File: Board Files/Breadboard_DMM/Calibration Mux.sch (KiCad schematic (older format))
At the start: 3 parts

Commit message: Finished main design, cleaning up schematic
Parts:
- added D?: 1N4007, Diode_SMD:D_SOD-123, symbol Device:D_ALT
- added K? (x2): EC2-5NU, Relay_THT:Relay_DPDT_Kemet_EC2, symbol irex_Relay:EC2-5NU_Split
- added Q? (x3): NTZD3154N, Package_TO_SOT_SMD:SOT-563, symbol irex_Transistor_FET:NTZD3154N
- added R? (x3): 10k, symbol Device:R_US
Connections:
- net +5VA: now also D?.1 (K), K?.1, R?.1, R?.1
- net GND: now also Q?.1 (S1), Q?.1 (S1), Q?.4 (S2), R?.2
- net INPUT_V+: now also K?.3; no longer U?.13 (X-COM)
- net CALIBRATE_MUX_A: no longer names the net of U?.10 (A)
- net CALIBRATE_MUX_A: now also Q?.6 (D1), R?.2
- net CALIBRATE_MUX_B: no longer names the net of U?.9 (B)
- net CALIBRATE_MUX_B: now also Q?.3 (D2), R?.2
- net CALIBRATE_MUX_INH: no longer names the net of R?.1, U?.6 (INH)
- new net: K?.5, U?.13 (X-COM)
- new net: D?.2 (A), K?.12, Q?.6 (D1)
- new net CALIBRATE_MUX_~A: Q?.2 (G1)
- new net CALIBRATE_MUX_~B: Q?.5 (G2)
- new net CALIBRATE_RELAY_ON: Q?.2 (G1), R?.1
- new net OUTPUT_V+: K?.4
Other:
- note added: "Calibration Input\nSelector"
- note added: "Calibration Relay Coil"
- note added: "~A"
- note added: "~B\n"
- note removed: "A"
- note removed: "B\n"
- moved on the sheet: C?, R?, U?

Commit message: Finished main cleanup, started adding digikey part numbers
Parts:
- C601: renamed from C?; Digi-Key PN (none) -> -
- D601: renamed from D?; Digi-Key PN (none) -> -
- K601: renamed from K?; Digi-Key PN (none) -> -
- Q601, Q602: renamed from Q?; Digi-Key PN (none) -> -
- R601, R602, R603, R604: renamed from R?; Digi-Key PN (none) -> -
- U601: renamed from U?; Digi-Key PN (none) -> -

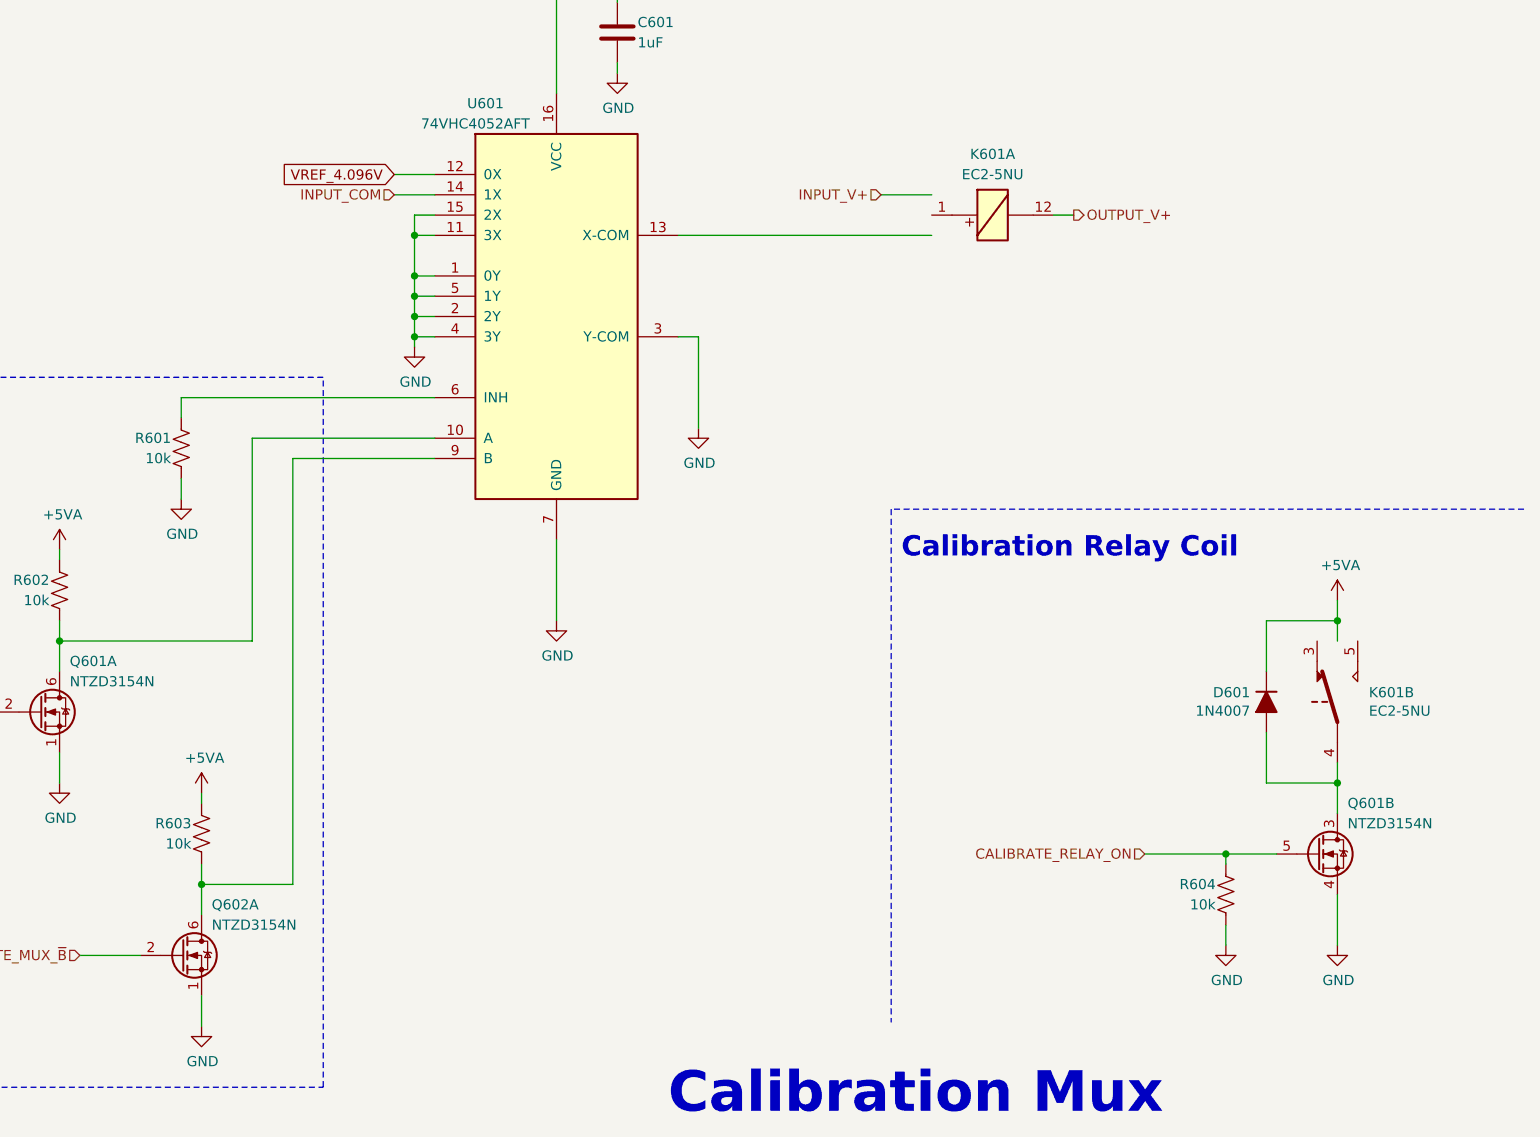
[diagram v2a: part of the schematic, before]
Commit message: Started adding Digikey links
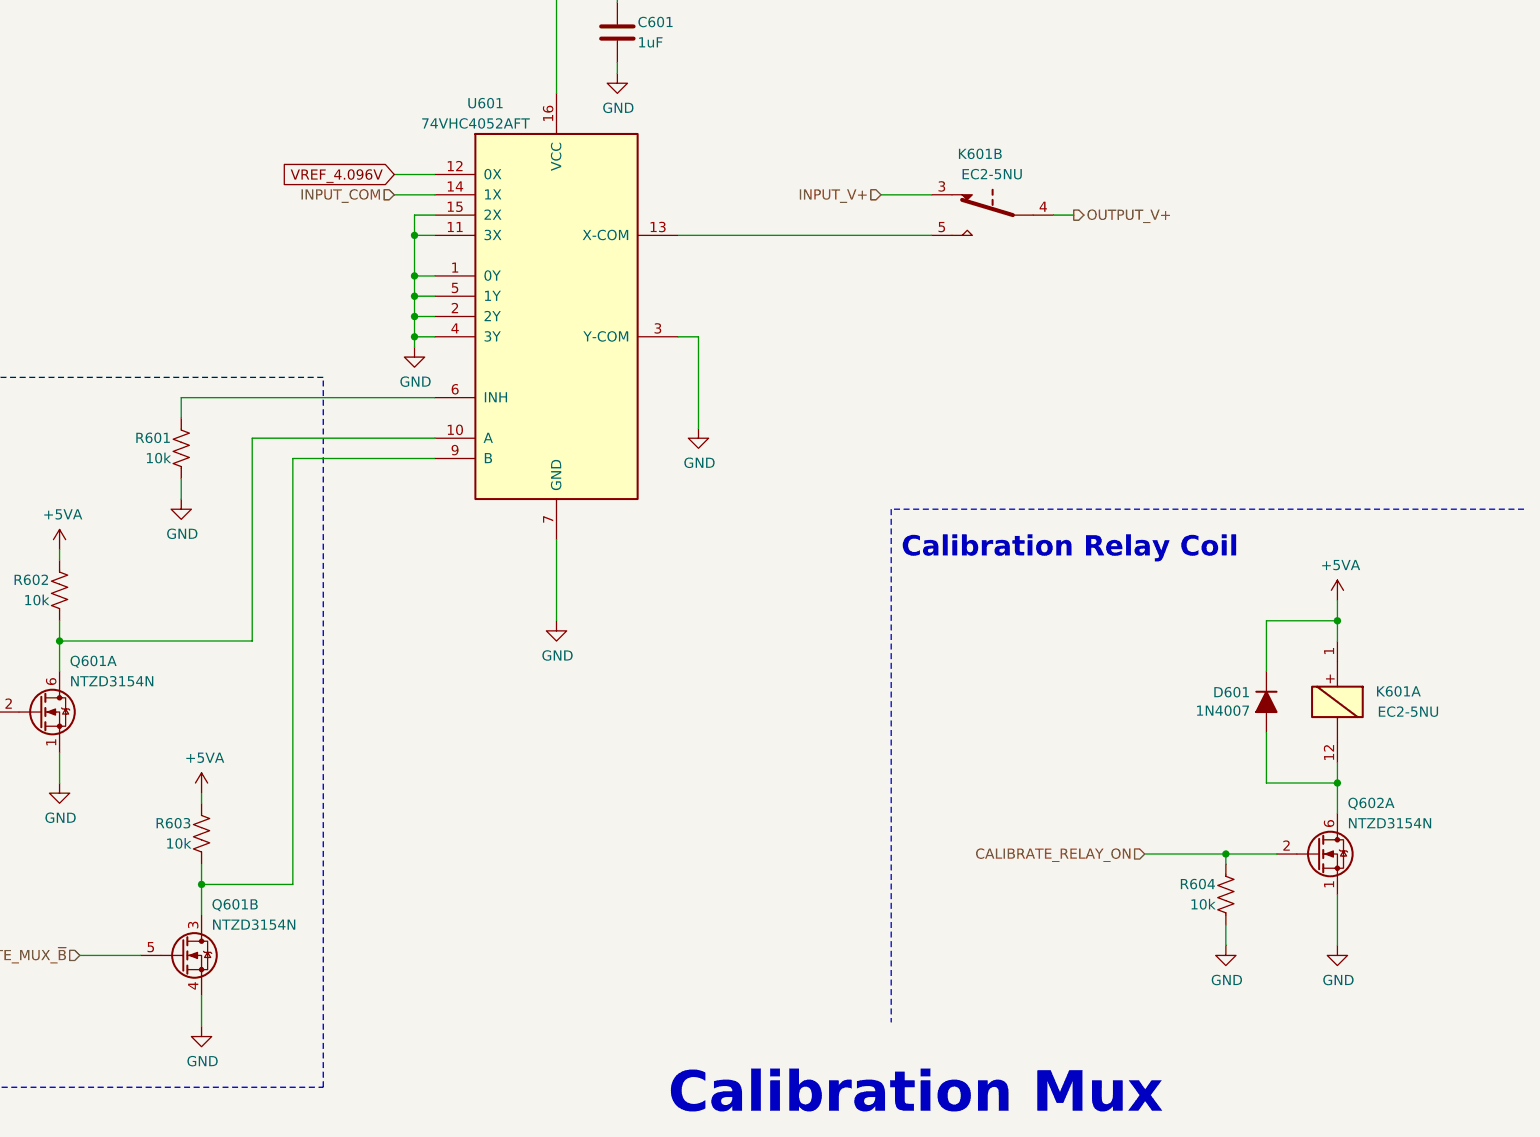
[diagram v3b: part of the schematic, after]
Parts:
- D601: Digi-Key Link (none) -> https://www.digikey.com/en/products/detail/smc-diode-soluti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; Digi-Key PN - -> 1655-1N4007FLCT-ND
- Q601: Digi-Key Link (none) -> https://www.digikey.com/en/products/detail/on-semiconductor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; Digi-Key PN - -> NTZD3154NT1GOSCT-ND
- Q601: renamed from Q602; Digi-Key Link (none) -> https://www.digikey.com/en/products/detail/on-semiconductor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; Digi-Key PN - -> NTZD3154NT1GOSCT-ND
- Q602: renamed from Q601; Digi-Key Link (none) -> https://www.digikey.com/en/products/detail/on-semiconductor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; Digi-Key PN - -> NTZD3154NT1GOSCT-ND
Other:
- moved on the sheet: K601A, K601B
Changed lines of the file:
@@
 $Descr USLetter 11000 8500
 encoding utf-8
-Sheet 5 10
+Sheet 6 11
 Title "Toast-O-Meter"
-Date ""
+Date "2020-08-14"
 Rev "0"
 Comp ""
@@
 $Comp
 L irex_Transistor_FET:NTZD3154N Q?
-U 1 1 5FFA77CB
+U 2 1 5FFA77CB
 P 4000 6450
 AR Path="/5F3FD151/5FFA77CB" Ref="Q?"  Part="2"
@@
 AR Path="/5F3FD151/5FEE79D7/5FFA77CB" Ref="Q?"  Part="2"
 AR Path="/5F511849/5F4FBB9F/5FEE8CDB/5FFA77CB" Ref="Q?"  Part="2"
-AR Path="/5F511849/5F4FBB9F/5FFA77CB" Ref="Q602"  Part="1"
-F 0 "Q602" H 4050 6700 50  0000 L CNN
+AR Path="/5F511849/5F4FBB9F/5FFA77CB" Ref="Q601"  Part="2"
+F 0 "Q601" H 4050 6700 50  0000 L CNN
 F 1 "NTZD3154N" H 4050 6600 50  0000 L CNN
 F 2 "Package_TO_SOT_SMD:SOT-563" H 4100 6350 50  0001 L CNN
 F 3 "https://www.onsemi.cn/PowerSolutions/document/NTZD3154N-D.PDF" H 4000 6450 50  0001 L CNN
-F 4 "" H 4000 6450 50  0001 C CNN "Digi-Key Link"
-F 5 "-" H 4000 6450 50  0001 C CNN "Digi-Key PN"
-	1    4000 6450
+F 4 "https://www.digikey.com/en/products/detail/on-semiconductor/NTZD3154NT1G/687137" H 4000 6450 50  0001 C CNN "Digi-Key Link"
+F 5 "NTZD3154NT1GOSCT-ND" H 4000 6450 50  0001 C CNN "Digi-Key PN"
+	2    4000 6450
 	1    0    0    -1
 $EndComp
@@
 F 2 "Package_TO_SOT_SMD:SOT-563" H 3400 5150 50  0001 L CNN
 F 3 "https://www.onsemi.cn/PowerSolutions/document/NTZD3154N-D.PDF" H 3300 5250 50  0001 L CNN
-F 4 "" H 3300 5250 50  0001 C CNN "Digi-Key Link"
-F 5 "-" H 3300 5250 50  0001 C CNN "Digi-Key PN"
+F 4 "https://www.digikey.com/en/products/detail/on-semiconductor/NTZD3154NT1G/687137" H 3300 5250 50  0001 C CNN "Digi-Key Link"
+F 5 "NTZD3154NT1GOSCT-ND" H 3300 5250 50  0001 C CNN "Digi-Key PN"
 	1    3300 5250
 	1    0    0    -1
@@
 $Comp
 L irex_Transistor_FET:NTZD3154N Q?
-U 2 1 5FFCC6C6
+U 1 1 5FFCC6C6
 P 9600 5950
 AR Path="/5F3FD151/5FFCC6C6" Ref="Q?"  Part="1"
@@
 AR Path="/5F511849/5F4FBB9F/5FEF5786/5FFCC6C6" Ref="Q?"  Part="1"
 AR Path="/5F511849/5F4FBB9F/5FEF9BAE/5FFCC6C6" Ref="Q?"  Part="1"
-AR Path="/5F511849/5F4FBB9F/5FFCC6C6" Ref="Q601"  Part="2"
-F 0 "Q601" H 9650 6200 50  0000 L CNN
+AR Path="/5F511849/5F4FBB9F/5FFCC6C6" Ref="Q602"  Part="1"
+F 0 "Q602" H 9650 6200 50  0000 L CNN
 F 1 "NTZD3154N" H 9650 6100 50  0000 L CNN
 F 2 "Package_TO_SOT_SMD:SOT-563" H 9700 5850 50  0001 L CNN
 F 3 "https://www.onsemi.cn/PowerSolutions/document/NTZD3154N-D.PDF" H 9600 5950 50  0001 L CNN
-F 4 "" H 9600 5950 50  0001 C CNN "Digi-Key Link"
-F 5 "-" H 9600 5950 50  0001 C CNN "Digi-Key PN"
-	2    9600 5950
+F 4 "https://www.digikey.com/en/products/detail/on-semiconductor/NTZD3154NT1G/687137" H 9600 5950 50  0001 C CNN "Digi-Key Link"
+F 5 "NTZD3154NT1GOSCT-ND" H 9600 5950 50  0001 C CNN "Digi-Key PN"
+	1    9600 5950
 	1    0    0    -1
 $EndComp
@@
 L irex_Relay:EC2-5NU_Split K?
 U 1 1 5FAFCC09
-P 7900 2800
+P 9600 5200
 AR Path="/5FAFCC09" Ref="K?"  Part="2"
 AR Path="/5F511849/5FAFCC09" Ref="K?"  Part="2"
 AR Path="/5F511849/5F4FBB9F/5FAFCC09" Ref="K601"  Part="1"
-F 0 "K601" V 7600 2800 50  0000 C CNN
-F 1 "EC2-5NU" V 7700 2800 50  0000 C CNN
+F 0 "K601" H 9300 5250 50  0000 C CNN
+F 1 "EC2-5NU" H 9250 5150 50  0000 C CNN
+F 2 "Relay_THT:Relay_DPDT_Kemet_EC2" H 9800 5100 50  0001 L CNN
+F 3 "https://content.kemet.com/datasheets/KEM_R7002_EC2_EE2.pdf" H 9600 5200 50  0001 C CNN
+F 4 "" H 9600 5200 50  0001 C CNN "Digi-Key Link"
+F 5 "-" H 9600 5200 50  0001 C CNN "Digi-Key PN"
+	1    9600 5200
+	-1   0    0    -1
+$EndComp
+$Comp
+L irex_Relay:EC2-5NU_Split K?
+U 2 1 5FAFCC0F
+P 7900 2800
+AR Path="/5FAFCC0F" Ref="K?"  Part="1"
+AR Path="/5F511849/5FAFCC0F" Ref="K?"  Part="1"
+AR Path="/5F511849/5F4FBB9F/5FAFCC0F" Ref="K601"  Part="2"
+F 0 "K601" V 7600 2750 50  0000 L CNN
+F 1 "EC2-5NU" V 7700 2650 50  0000 L CNN
 F 2 "Relay_THT:Relay_DPDT_Kemet_EC2" H 8100 2700 50  0001 L CNN
 F 3 "https://content.kemet.com/datasheets/KEM_R7002_EC2_EE2.pdf" H 7900 2800 50  0001 C CNN
 F 4 "" H 7900 2800 50  0001 C CNN "Digi-Key Link"
 F 5 "-" H 7900 2800 50  0001 C CNN "Digi-Key PN"
-	1    7900 2800
+	2    7900 2800
 	0    -1   1    0
-$EndComp
-$Comp
-L irex_Relay:EC2-5NU_Split K?
-U 2 1 5FAFCC0F
-P 9600 5200
-AR Path="/5FAFCC0F" Ref="K?"  Part="1"
-AR Path="/5F511849/5FAFCC0F" Ref="K?"  Part="1"
-AR Path="/5F511849/5F4FBB9F/5FAFCC0F" Ref="K601"  Part="2"
-F 0 "K601" H 9755 5246 50  0000 L CNN
-F 1 "EC2-5NU" H 9755 5155 50  0000 L CNN
-F 2 "Relay_THT:Relay_DPDT_Kemet_EC2" H 9800 5100 50  0001 L CNN
-F 3 "https://content.kemet.com/datasheets/KEM_R7002_EC2_EE2.pdf" H 9600 5200 50  0001 C CNN
-F 4 "" H 9600 5200 50  0001 C CNN "Digi-Key Link"
-F 5 "-" H 9600 5200 50  0001 C CNN "Digi-Key PN"
-	2    9600 5200
-	1    0    0    -1
 $EndComp
 $Comp
@@
 F 2 "Diode_SMD:D_SOD-123" H 9250 5200 50  0001 C CNN
 F 3 "http://www.smc-diodes.com/propdf/1N4001FL-1N4007FL%20N1646%20REV.A.pdf" H 9250 5200 50  0001 C CNN
-F 4 "" H 9250 5200 50  0001 C CNN "Digi-Key Link"
-F 5 "-" H 9250 5200 50  0001 C CNN "Digi-Key PN"
+F 4 "https://www.digikey.com/en/products/detail/smc-diode-solutions/1N4007FLTR/11657817" H 9250 5200 50  0001 C CNN "Digi-Key Link"
+F 5 "1655-1N4007FLCT-ND" H 9250 5200 50  0001 C CNN "Digi-Key PN"
 	1    9250 5200
 	0    -1   1    0

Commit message: Finished adding parts, cleaned up, ran ERC
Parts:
- added unit 2 of Q602
- added R603, R605, R606: 100, Resistor_SMD:R_0603_1608Metric_Pad1.05x0.95mm_HandSolder, symbol Device:R_US
- C601: footprint (none) -> Resistor_SMD:R_0603_1608Metric_Pad1.05x0.95mm_HandSolder; Digi-Key Link (none) -> https://www.digikey.com/en/products/detail/samsung-electro-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; Digi-Key PN - -> 1276-6524-1-ND
- K601: Digi-Key Link (none) -> https://www.digikey.com/en/products/detail/kemet/EC2-5NU/42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; Digi-Key PN - -> 399-11052-5-ND
- R601, R602: footprint (none) -> Resistor_SMD:R_0603_1608Metric_Pad1.05x0.95mm_HandSolder; Digi-Key Link (none) -> https://www.digikey.com/en/products/detail/yageo/RC0603FR-0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; Digi-Key PN - -> 311-10.0KHRCT-ND
- R604: renamed from R603; footprint (none) -> Resistor_SMD:R_0603_1608Metric_Pad1.05x0.95mm_HandSolder; Digi-Key Link (none) -> https://www.digikey.com/en/products/detail/yageo/RC0603FR-0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; Digi-Key PN - -> 311-10.0KHRCT-ND
- R607: renamed from R604; footprint (none) -> Resistor_SMD:R_0603_1608Metric_Pad1.05x0.95mm_HandSolder; Digi-Key Link (none) -> https://www.digikey.com/en/products/detail/yageo/RC0603FR-0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; Digi-Key PN - -> 311-10.0KHRCT-ND
- U601: Digi-Key Link (none) -> https://www.digikey.com/en/products/detail/toshiba-semicond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; Digi-Key PN - -> 74VHC4052AFTCT-ND
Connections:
- net CALIBRATE_MUX_~A: now also R603.1; no longer Q601.2 (G1)
- net CALIBRATE_MUX_~B: now also R606.1; no longer Q601.5 (G2)
- net CALIBRATE_RELAY_ON: now also R605.1; no longer Q602.2 (G1), R607.1
- net GND: now also Q602.3 (D2), Q602.4 (S2), Q602.5 (G2)
- new net: Q601.5 (G2), R606.2
- new net: Q601.2 (G1), R603.2
- new net: Q602.2 (G1), R605.2, R607.1
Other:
- moved on the sheet: C601, D601, K601A, K601B, Q601A, Q601B, Q602A, R601, R602, R604, R607, U601

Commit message: Updated probe connector arrangement
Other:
- note removed: "Calibration Mux"
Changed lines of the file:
@@
 Sheet 5 8
 Title "Toast-O-Meter"
-Date "2020-08-14"
+Date "2020-10-06"
 Rev "0"
 Comp ""
-Comment1 ""
+Comment1 "Isaac Rex"
 Comment2 ""
 Comment3 ""
 Comment4 ""
 $EndDescr
-Text Notes 12450 9700 0    200  ~ 40
-Calibration Mux
 Text Notes 4350 6250 0    50   ~ 0
 GND
@@
 Wire Wire Line
 	15050 8400 15300 8400
-Wire Notes Line
-	16520 6700 13400 6700
-Wire Notes Line
-	13400 6700 13400 9230
 $Comp
 L Device:R_US R?
@@
 	13950 7150 13950 7250
 Connection ~ 13550 7450
+Wire Notes Line
+	16500 6650 13200 6650
+Wire Notes Line
+	13200 6650 13200 9550
 $EndSCHEMATC

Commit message: Semi-finished component placement
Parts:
- C501: renamed from C601; footprint Resistor_SMD:R_0603_1608Metric_Pad1.05x0.95mm_HandSolder -> Capacitor_SMD:C_0603_1608Metric_Pad1.08x0.95mm_HandSolder
- D501: renamed from D601; symbol Device:D_ALT -> Device:D_Filled
- K501: renamed from K601; MPN (none) -> EC2-5NU
- Q501: renamed from Q601; value NTZD3154N -> BSD840N; footprint Package_TO_SOT_SMD:SOT-563 -> Package_TO_SOT_SMD:SOT-363_SC-70-6_Handsoldering; Digi-Key Link https://www.digikey.com/en/products/detail/on-semiconductor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 -> https://www.digikey.com/en/products/detail/infineon-technol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; Digi-Key PN NTZD3154NT1GOSCT-ND -> BSD840NH6327XTSA1CT-ND; MPN (none) -> BSD840NH6327XTSA1
- Q502: renamed from Q602; value NTZD3154N -> BSD840N; footprint Package_TO_SOT_SMD:SOT-563 -> Package_TO_SOT_SMD:SOT-363_SC-70-6_Handsoldering; Digi-Key Link https://www.digikey.com/en/products/detail/on-semiconductor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 -> https://www.digikey.com/en/products/detail/infineon-technol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; Digi-Key PN NTZD3154NT1GOSCT-ND -> BSD840NH6327XTSA1CT-ND; MPN (none) -> BSD840NH6327XTSA1
- renumbered R601 to R501, R602 to R502, R603 to R503, R604 to R504, R605 to R505, R606 to R506, R607 to R507, U601 to U501
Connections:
- net at R502.2, U501.10 (A): now also Q501.3 (D2); no longer Q501.6 (D1)
- net at R504.2, U501.9 (B): now also Q501.6 (D1); no longer Q501.3 (D2)
- net at R506.2: now also Q501.2 (G1); no longer Q501.5 (G2)
- net at R503.2: now also Q501.5 (G2); no longer Q501.2 (G1)
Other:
- moved on the sheet: Q501A, Q501B
